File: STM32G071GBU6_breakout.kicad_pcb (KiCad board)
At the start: 2 copper layers, 39.4 x 16.5 mm, 14 parts, among them J1 Conn_01x14, J2 Conn_01x14, J3 Conn_01x04, SW1 SW_Push, U1 MCP1700-3302E_SOT23, U2 STM32G071GBU6

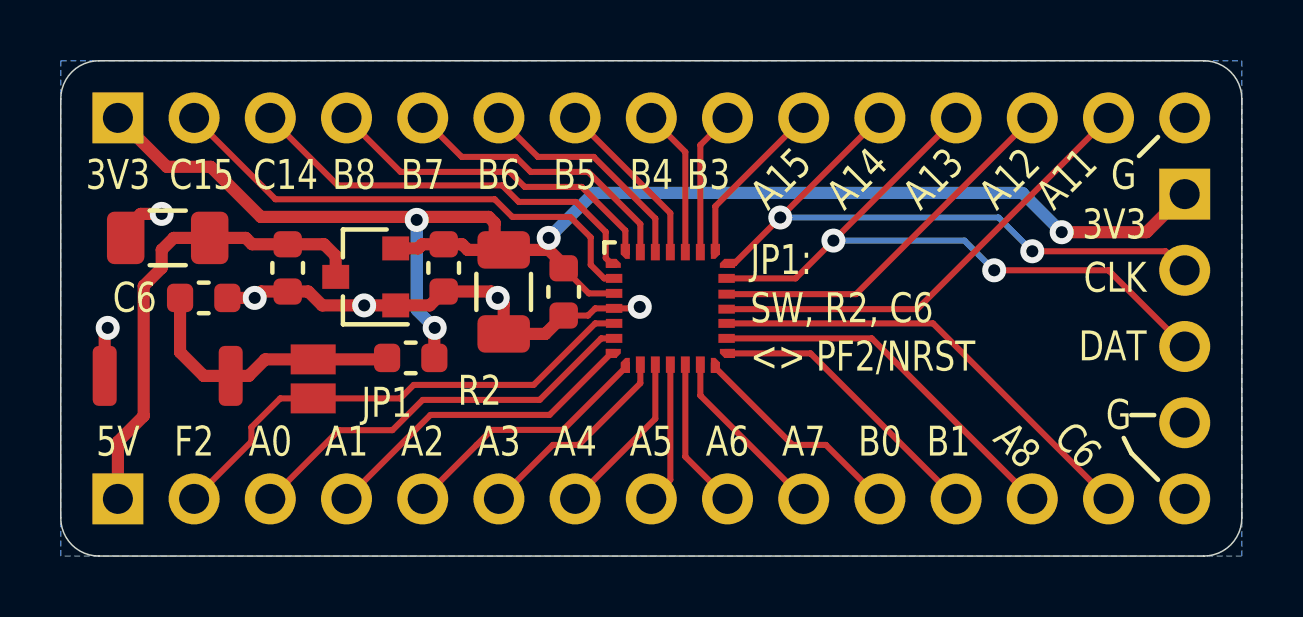
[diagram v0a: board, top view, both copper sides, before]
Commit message: change SW to KMR2
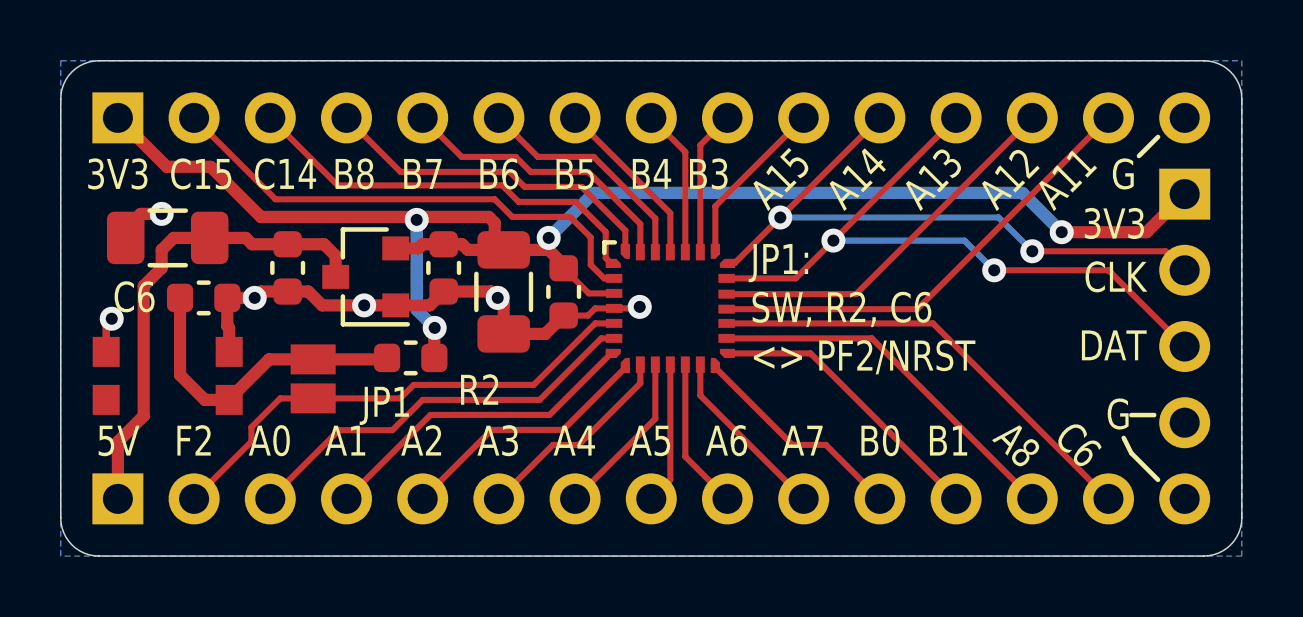
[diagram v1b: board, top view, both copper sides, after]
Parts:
- SW1: footprint Button_Switch_SMD:SW_Push_SPST_NO_Alps_SKRK -> Button_Switch_SMD:SW_Push_1P1T_NO_CK_KMR2
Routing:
- net GND: track 19.3 -> 20.6 mm
- net Net-(C6-Pad1): track 9.32 -> 10.4 mm
